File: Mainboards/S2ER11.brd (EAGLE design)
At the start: 43 x 72 mm, 52 parts, among them IC1 LD1117S33, IC2 CC1101RTK, IC3 STM32F051C8, Q1 IRLML9301, Q2 8M, X1 VCC, X2 CLK, X3 GND, X4 DIO, X5 RST, X6 NC

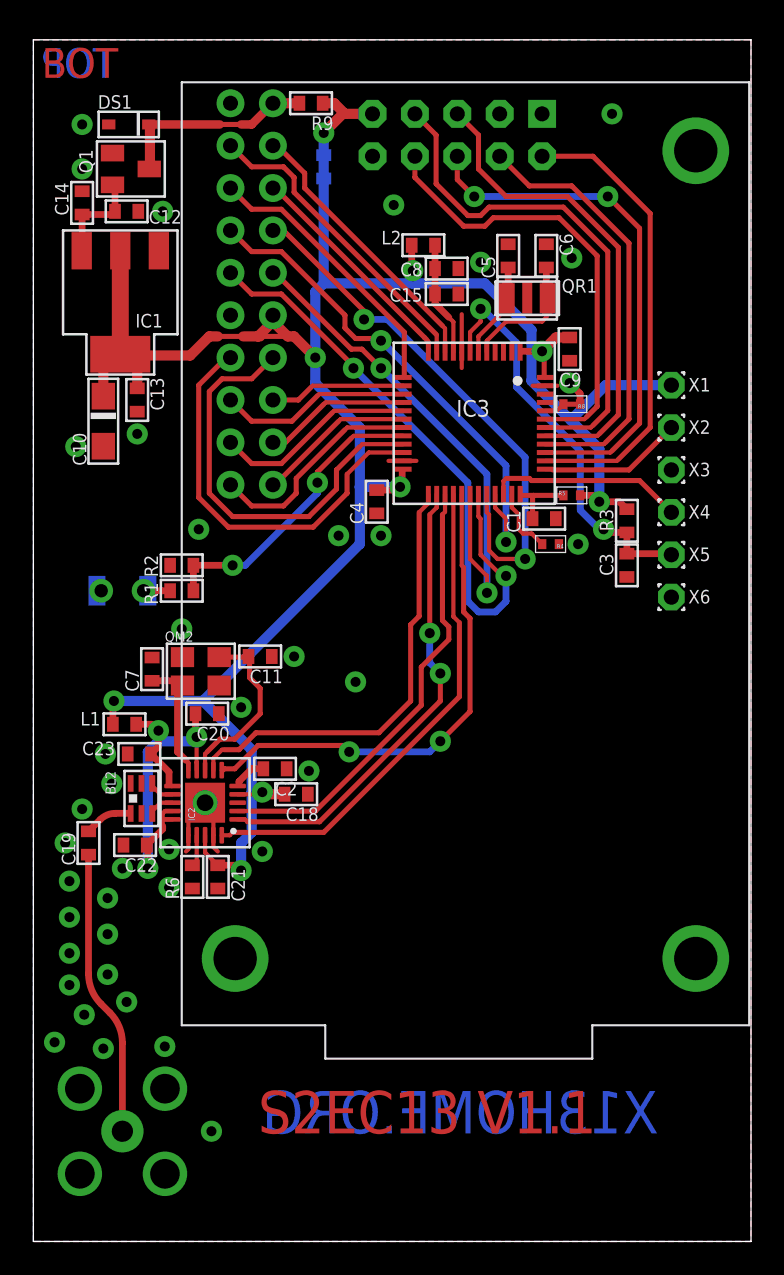
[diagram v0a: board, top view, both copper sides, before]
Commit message: Added prototypes
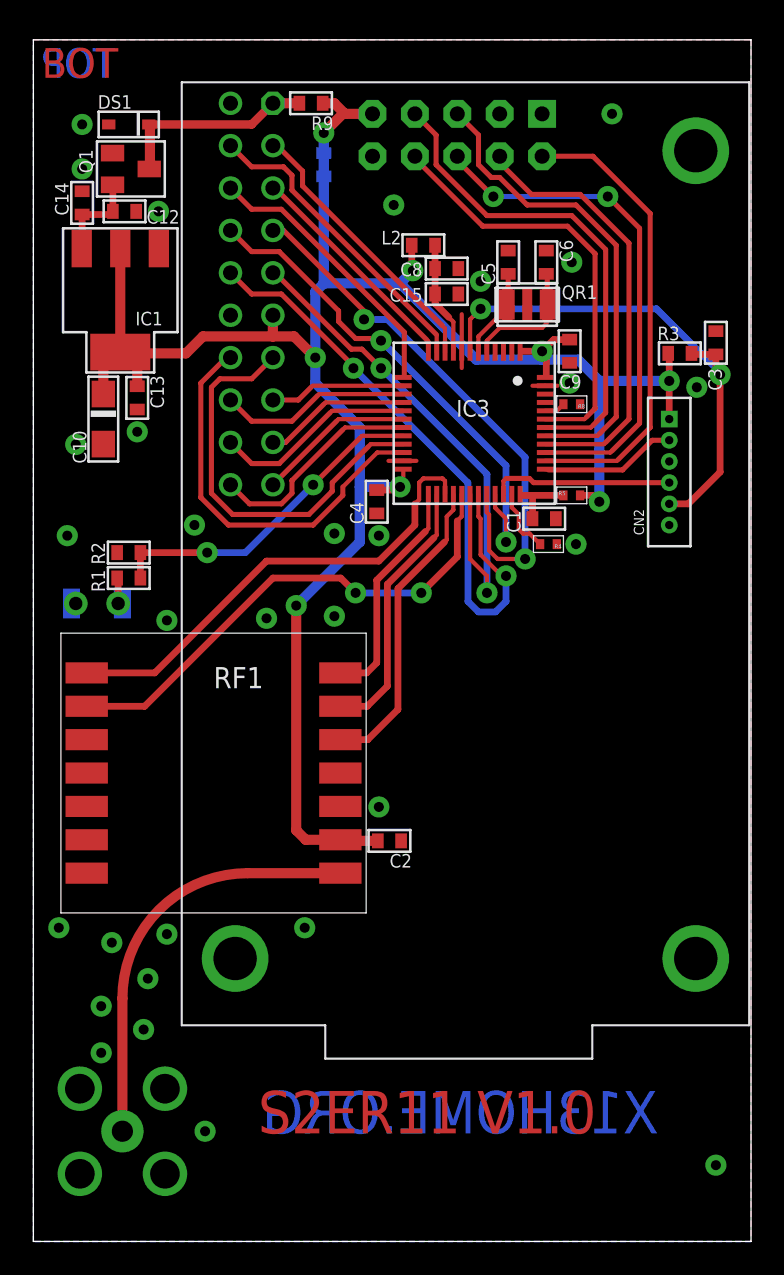
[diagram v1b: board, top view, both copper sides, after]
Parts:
- removed ANT: SMA-BU, Conn:BU-SMA-V
- removed BL2: 0896BM15A0001, RF:BL
- removed C11, C7: 22p, RCL:0603
- removed C18, C20, C21, C22, C23: 100n, RCL:0603
- removed C19: 100p, RCL:0603
- removed IC2: CC1101RTK, RF:VQFN20
- removed L1: 10uH, RCL:0603
- removed QM2: 26M, QUARTZ:SMD_4P_3.2X2.5
- removed R6: 56k, RCL:0603
- removed X1: VCC, Conn:T1.6/0.9
- removed X2: CLK, Conn:T1.6/0.9
- removed X4: DIO, Conn:T1.6/0.9
- removed X5: RST, Conn:T1.6/0.9
- removed X6: NC, Conn:T1.6/0.9
- added CN2: SWD, Conn:CON6L
- added RF1: RFM69CW, RF:RFM12B
- X3: value GND -> SMA-BU; device Conn:T1.6/0.9 -> Conn:BU-SMA-V
- moved X3 51.5 mm to (5.33, 6.60), flipped to the bottom
- moved C3 14.4 mm to (40.9, 53.8), turned to 90 degrees
- moved R3 10.5 mm to (38.7, 53.2), turned to 0 degrees
- moved C2 8.10 mm to (21.3, 24.0)
- moved R1 3.27 mm to (5.71, 39.8)
- moved R2 3.27 mm to (5.71, 41.3)
- moved LED1 1.70 mm to (3.81, 38.2)
- moved LED2 1.70 mm to (3.81, 38.2)
- moved C5 0.38 mm to (28.4, 58.7)
- moved C6 0.38 mm to (30.7, 58.7)
- moved Q2 0.38 mm to (29.6, 56.1)
- moved QR1 0.38 mm to (29.6, 56.1)
- moved R7 0.13 mm to (17.4, 64.5)
- moved C10 0.13 mm to (4.19, 49.3)
- moved C13 0.13 mm to (6.22, 50.5)
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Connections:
- removed net N$11: C11.2, IC2.-8, QM2.3
- removed net N$12: C7.1, IC2.-10, QM2.1
- removed net N$13: BL2.1, C19.1
- removed net N$14: ANT.1, C19.2
- removed net N$6: IC2.-17, R6.2
- removed net N$7: C2.2, IC2.-5
- removed net N$8: BL2.3, IC2.-13
- removed net N$9: BL2.4, IC2.-12
- removed net VDD: C20.2, C22.2, C23.2, IC2.-11, IC2.-14, IC2.-15, IC2.-9, L1.1
- new net N$5: RF1.ANT, X3.1
- net +3V3: now also C2.2, CN2.1, RF1.VDD; no longer C18.2, C21.2, IC2.-18, IC2.-4, L1.2, X1.1
- net GND: now also CN2.3, RF1.GND, RF1.GND@1, X3.2, X3.3, X3.4, X3.5; no longer ANT.2, ANT.3, ANT.4, ANT.5, BL2.2, BL2.5, BL2.6, C11.1, C18.1, C20.1, C21.1, C22.1, C23.1, C7.2, IC2.-16, IC2.-19, IC2.P, QM2.2, QM2.4, R6.1, X3.1
- net RST: now also CN2.5; no longer X5.1
- net R_IRQ: now also RF1.IRQ; no longer IC2.-6
- net R_MISO: now also RF1.SDO; no longer IC2.-2
- net R_MOSI: now also RF1.SDI; no longer IC2.-20
- net R_NSS: now also RF1.SEL; no longer IC2.-7
- net R_SCK: now also RF1.SCK; no longer IC2.-1
- net SWCLK: now also CN2.2; no longer X2.1
- net SWDIO: now also CN2.4; no longer X4.1
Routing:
- net VDD: track 24.9 -> 0.00 mm, vias 3 -> 0
- net N$5: track 1.02 -> 24.1 mm
- net N$14: track 17.1 -> 0.00 mm
- net +3V3: track 145.7 -> 129.6 mm, vias 9 -> 8
- net R_NSS: track 26.8 -> 13.8 mm
- net R_SCK: track 28.0 -> 16.0 mm, vias 2 -> 0
- net R_MOSI: track 30.0 -> 18.5 mm
- net N$11: track 10.8 -> 0.00 mm
- net N$12: track 7.40 -> 0.00 mm
- net GND: track 13.0 -> 6.37 mm, vias 41 -> 30
- net RST: track 24.8 -> 31.4 mm
- net N$13: track 2.89 -> 0.00 mm
- net LED: track 18.1 -> 20.2 mm
- net N$7: track 2.08 -> 0.00 mm
- net N$6: track 1.91 -> 0.00 mm
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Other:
- board text added: "S2ER11 V1.0"
- board text removed: "S2EC13 V1.1"
